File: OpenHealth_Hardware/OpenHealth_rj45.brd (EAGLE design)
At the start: 119.4 x 32.7 mm, 7 parts

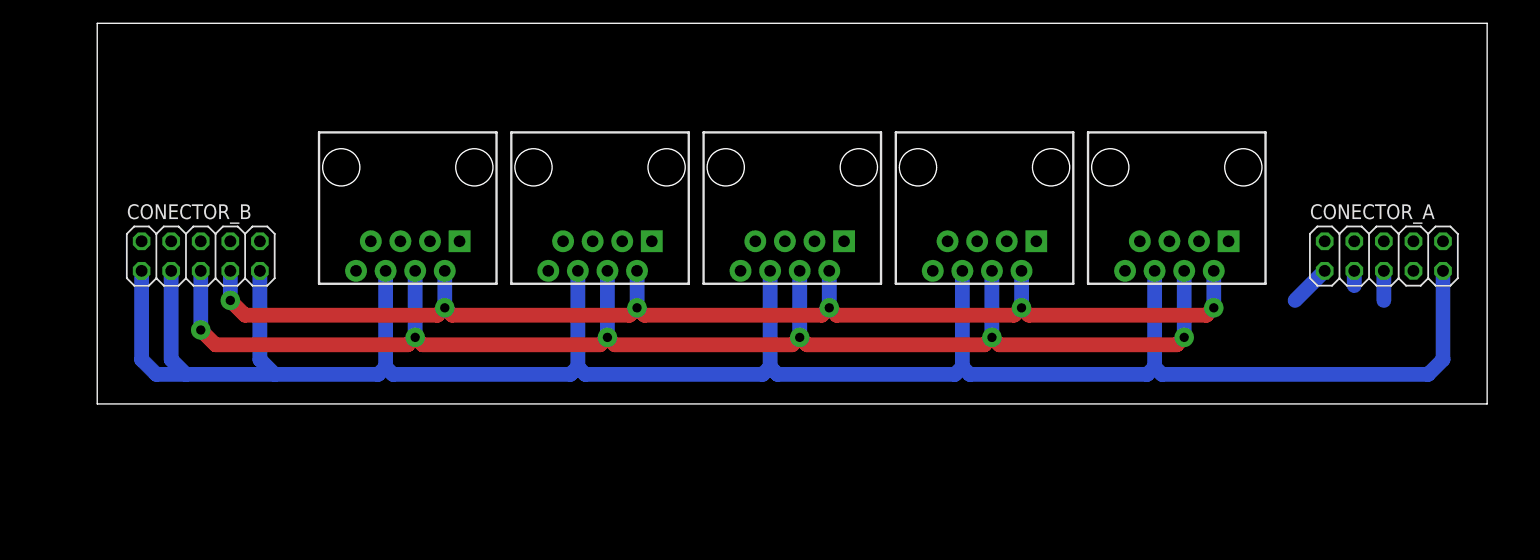
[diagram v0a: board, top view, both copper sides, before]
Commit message: Enrutado del de la placa de los conectores del RJ45 y se comienzo del proceso de ordenamiento de la placa principal
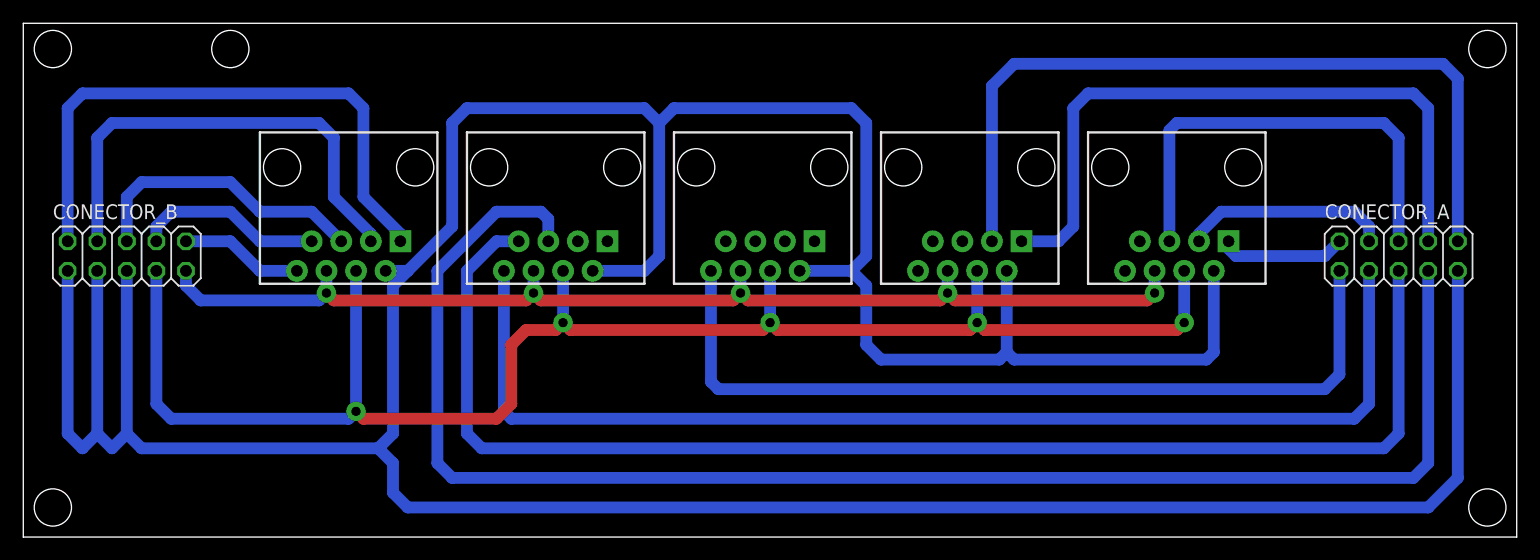
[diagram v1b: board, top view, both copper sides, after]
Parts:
- moved CONECTOR_B 6.35 mm to (12.7, 80.0)
- moved PESO 5.08 mm to (31.8, 87.6)
- moved PRESION_SANGUINEA 3.81 mm to (49.5, 87.6)
- moved TEMPERATURA 2.54 mm to (67.3, 87.6)
- moved ALTURA 1.27 mm to (85.1, 87.6)
- moved CONECTOR_A 1.27 mm to (121.9, 80.0)
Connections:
- net 3.3V: now also ALTURA.4, ELECTROCARDIOGRAMA.4, PESO.4, PRESION_SANGUINEA.4, TEMPERATURA.4; no longer ALTURA.2, ELECTROCARDIOGRAMA.2, PESO.2, PRESION_SANGUINEA.2, TEMPERATURA.2
- net D11: now also ALTURA.1; no longer ALTURA.7
- net D12: now also ALTURA.3; no longer ALTURA.8
- net GND: now also ALTURA.2, CONECTOR_B.5, ELECTROCARDIOGRAMA.2, PESO.2, PRESION_SANGUINEA.2, TEMPERATURA.2; no longer ALTURA.6, CONECTOR_B.9, ELECTROCARDIOGRAMA.6, PESO.6, PRESION_SANGUINEA.6, TEMPERATURA.6
- net LA: now also ELECTROCARDIOGRAMA.3; no longer ELECTROCARDIOGRAMA.7
- net RL: now also ELECTROCARDIOGRAMA.1; no longer ELECTROCARDIOGRAMA.8
- net VIN: now also ALTURA.6, CONECTOR_B.9, ELECTROCARDIOGRAMA.6, PESO.6, PRESION_SANGUINEA.6, TEMPERATURA.6; no longer ALTURA.4, CONECTOR_B.5, ELECTROCARDIOGRAMA.4, PESO.4, PRESION_SANGUINEA.4, TEMPERATURA.4
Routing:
- net GND: track 190.8 -> 343.8 mm
- net BPM_RX: track 0.00 -> 133.0 mm
- net BPM_TX: track 2.54 -> 114.5 mm
- net SALIDA_D6: track 1.27 -> 98.6 mm
- net A0: track 3.59 -> 73.2 mm
- net D12: track 0.00 -> 68.6 mm
- net D11: track 0.00 -> 58.1 mm
- net LCA_YLW: track 0.00 -> 50.6 mm
- net LCA_GRN: track 0.00 -> 40.5 mm
- net RA: track 0.00 -> 38.9 mm
- net 3.3V: track 105.8 -> 138.6 mm, vias 6 -> 5
- net LCA_WHT: track 0.00 -> 24.9 mm
- net VIN: track 121.0 -> 96.9 mm, vias 6 -> 5
- net LA: track 0.00 -> 17.8 mm
- net LCA_BLK: track 0.00 -> 16.2 mm
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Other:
- board size 119.4 x 32.7 mm -> 128.2 x 44.1 mm
